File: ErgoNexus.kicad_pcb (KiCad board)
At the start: 2 copper layers, 174.3 x 138 mm, 110 parts, among them J7 Conn_01x02, J8 Conn_01x02, SW1 SW_Push, SW2 RotaryEncoder_Switch, SW3 SW_Push, SW4 RotaryEncoder_Switch, U1 SuperMini nRF52840, U2 SuperMini nRF52840

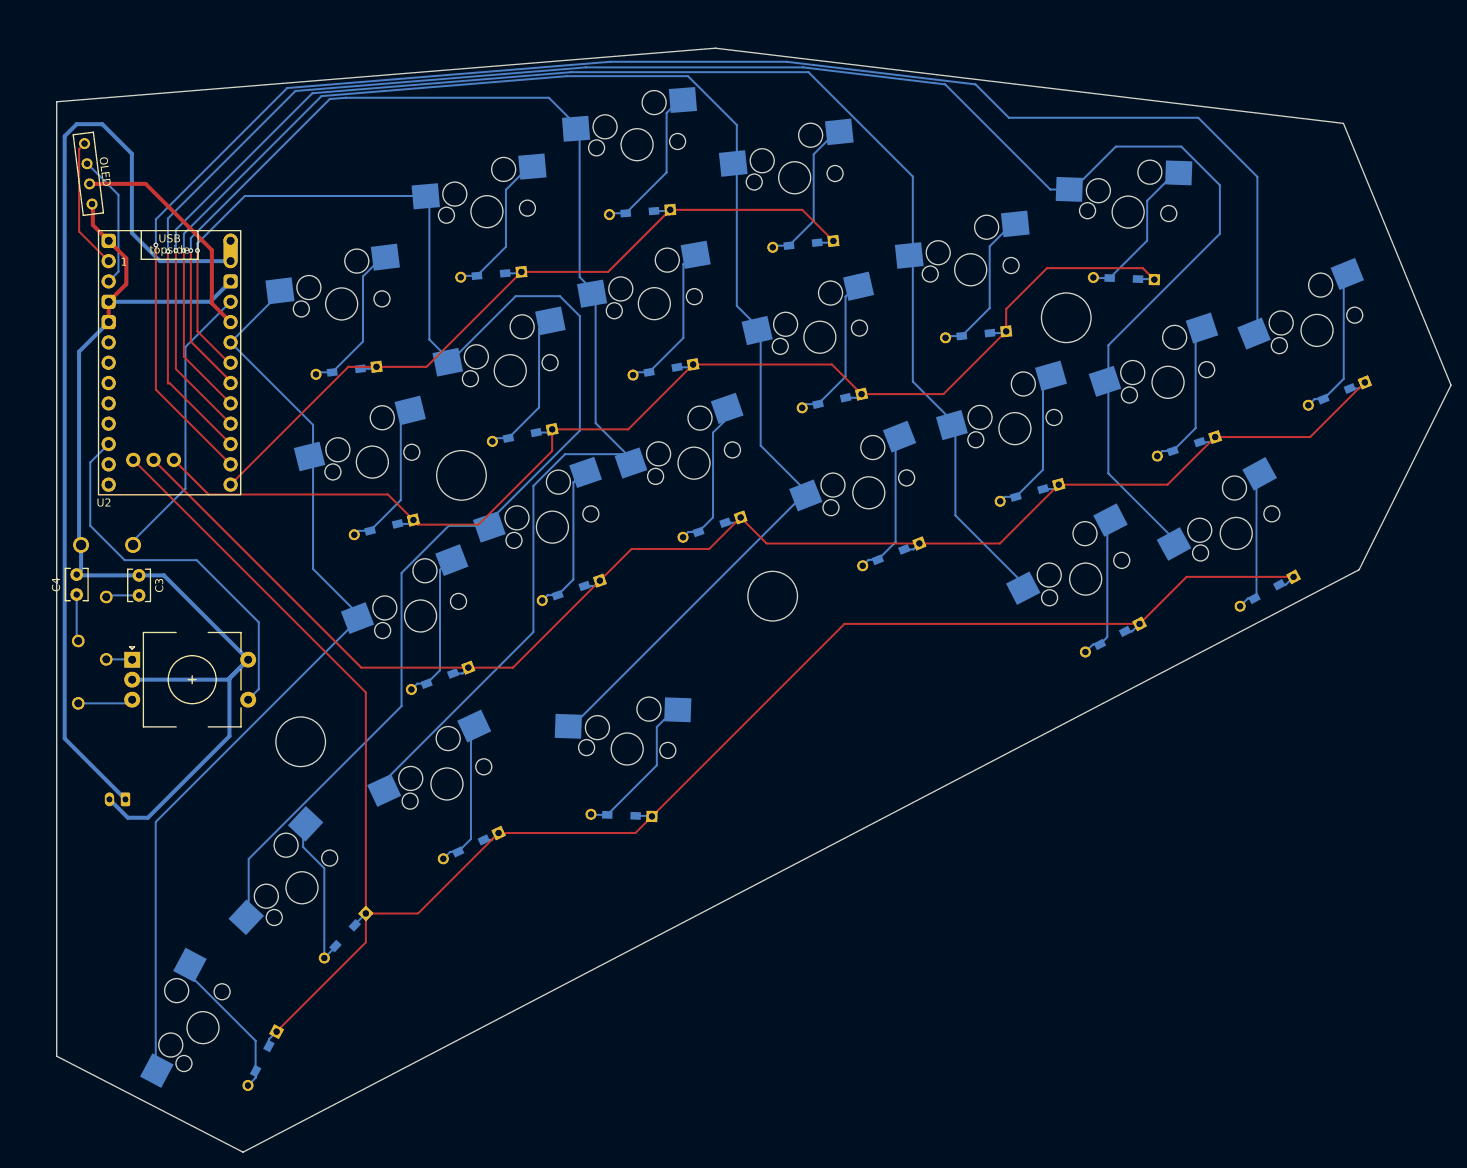
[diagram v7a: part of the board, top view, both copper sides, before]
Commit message: fix: 外形の変更
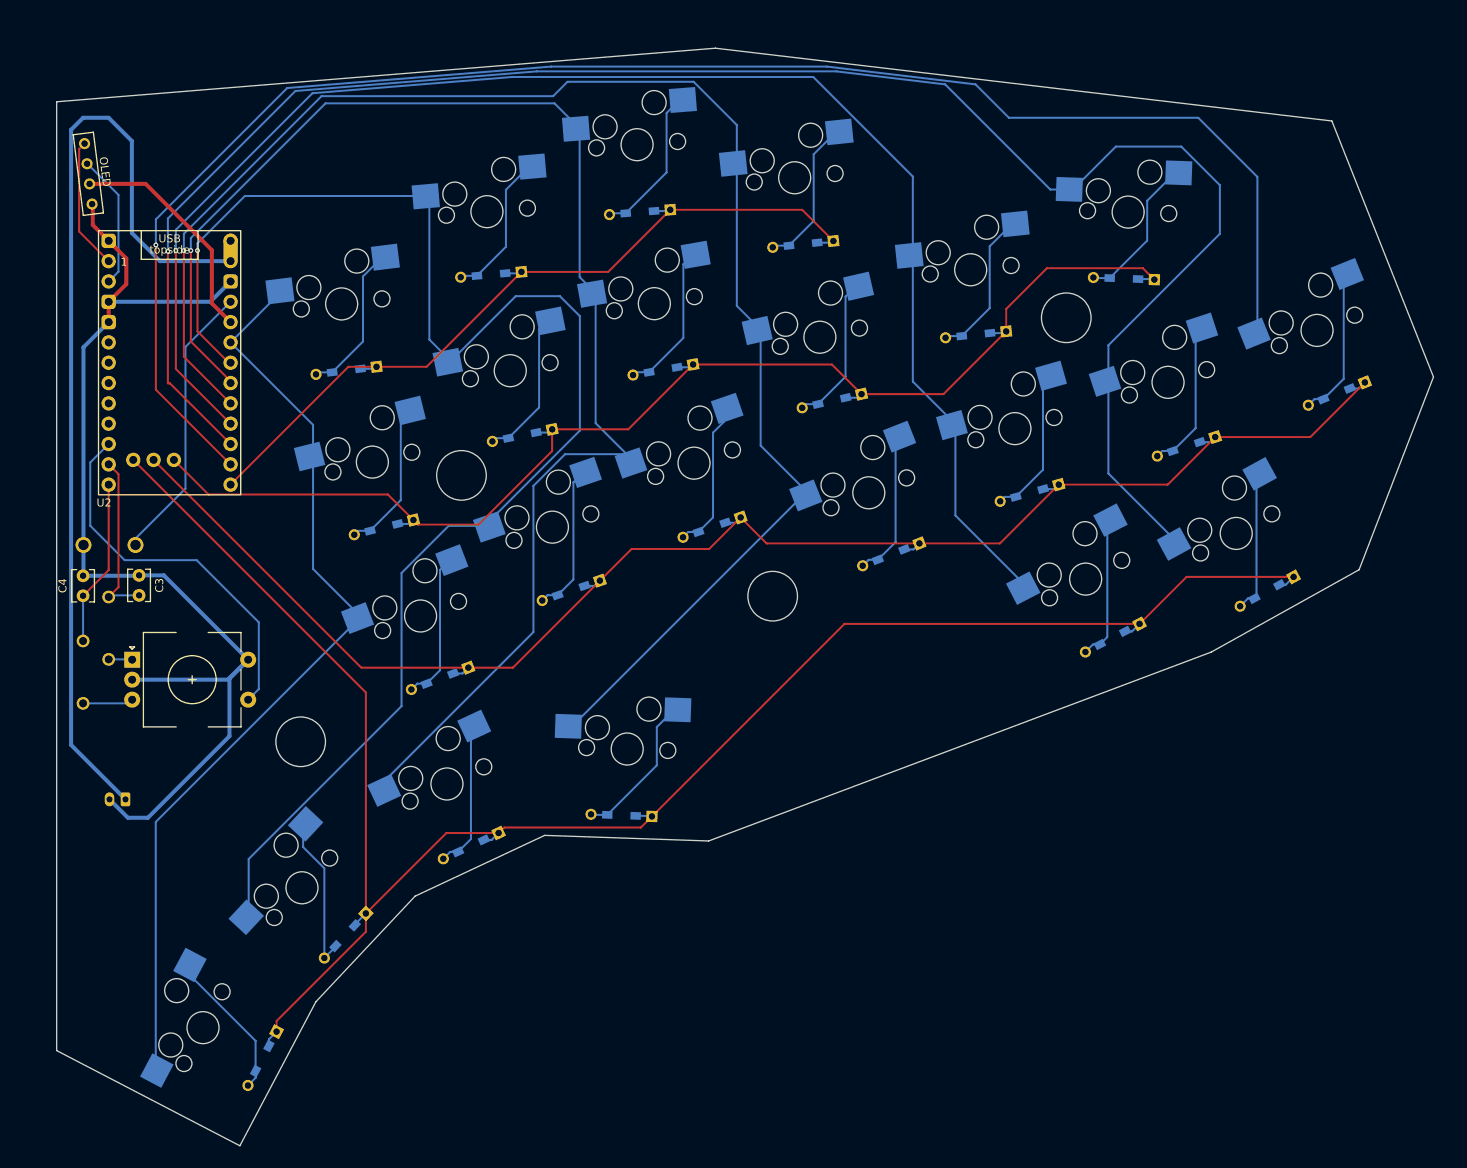
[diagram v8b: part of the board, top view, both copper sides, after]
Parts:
- moved C4 0.81 mm to (229.7, 130.1)
- moved R4 0.60 mm to (229.7, 139.7)
- moved SW3 0.30 mm to (233.0, 123.8)
- moved R3 0.30 mm to (232.9, 134.2)
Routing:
- net Ro_A_R: track 3.90 -> 21.5 mm
- net Ro_B_R: track 5.60 -> 20.9 mm
- net BAT_R: track 120.3 -> 121.2 mm
- net GND_R: track 138.7 -> 138.0 mm
- net Col3_R: track 179.3 -> 178.8 mm
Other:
- board size 174.3 x 138 mm -> 172.1 x 137.2 mm
